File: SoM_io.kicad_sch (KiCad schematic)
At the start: 1 part, among them J1 Hermaphroditic_Molex_203456-0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

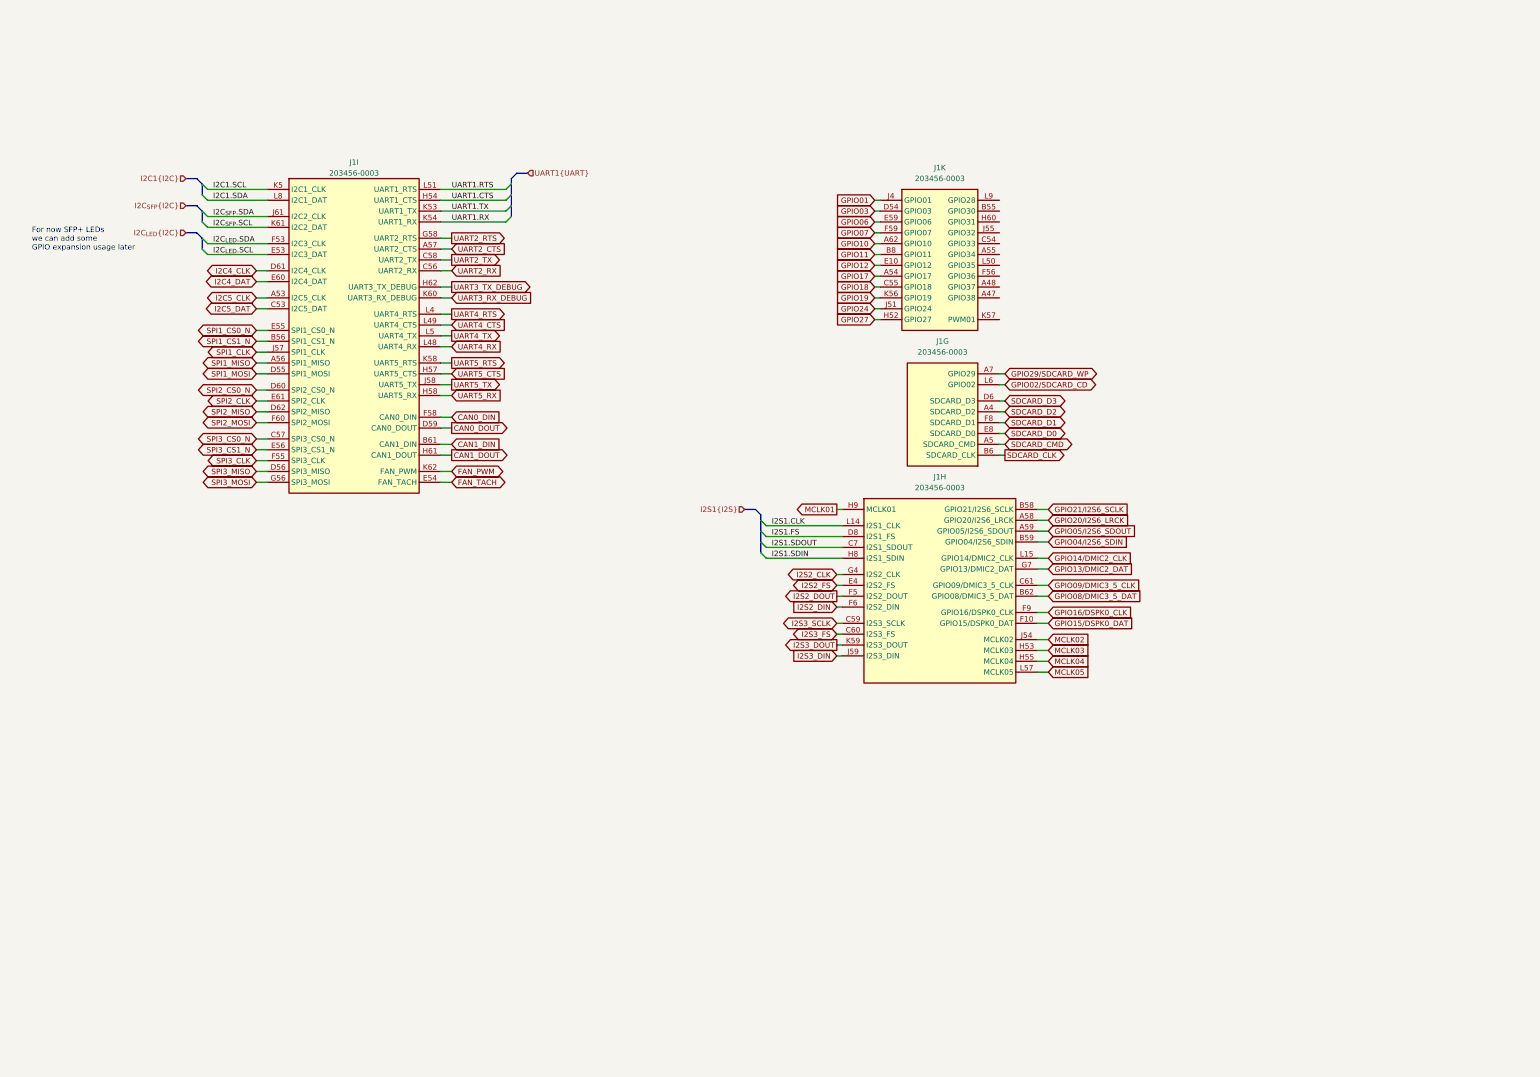
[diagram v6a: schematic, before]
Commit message: [#81970] Finalize connecting SFP+ to SOM
[#82054] Update SoM pins definitions

[#82054] Continue work on I2C

[#82330] Clean up

[#81970] Add SFP sheet and power section

[#82330] Annotation and clean up
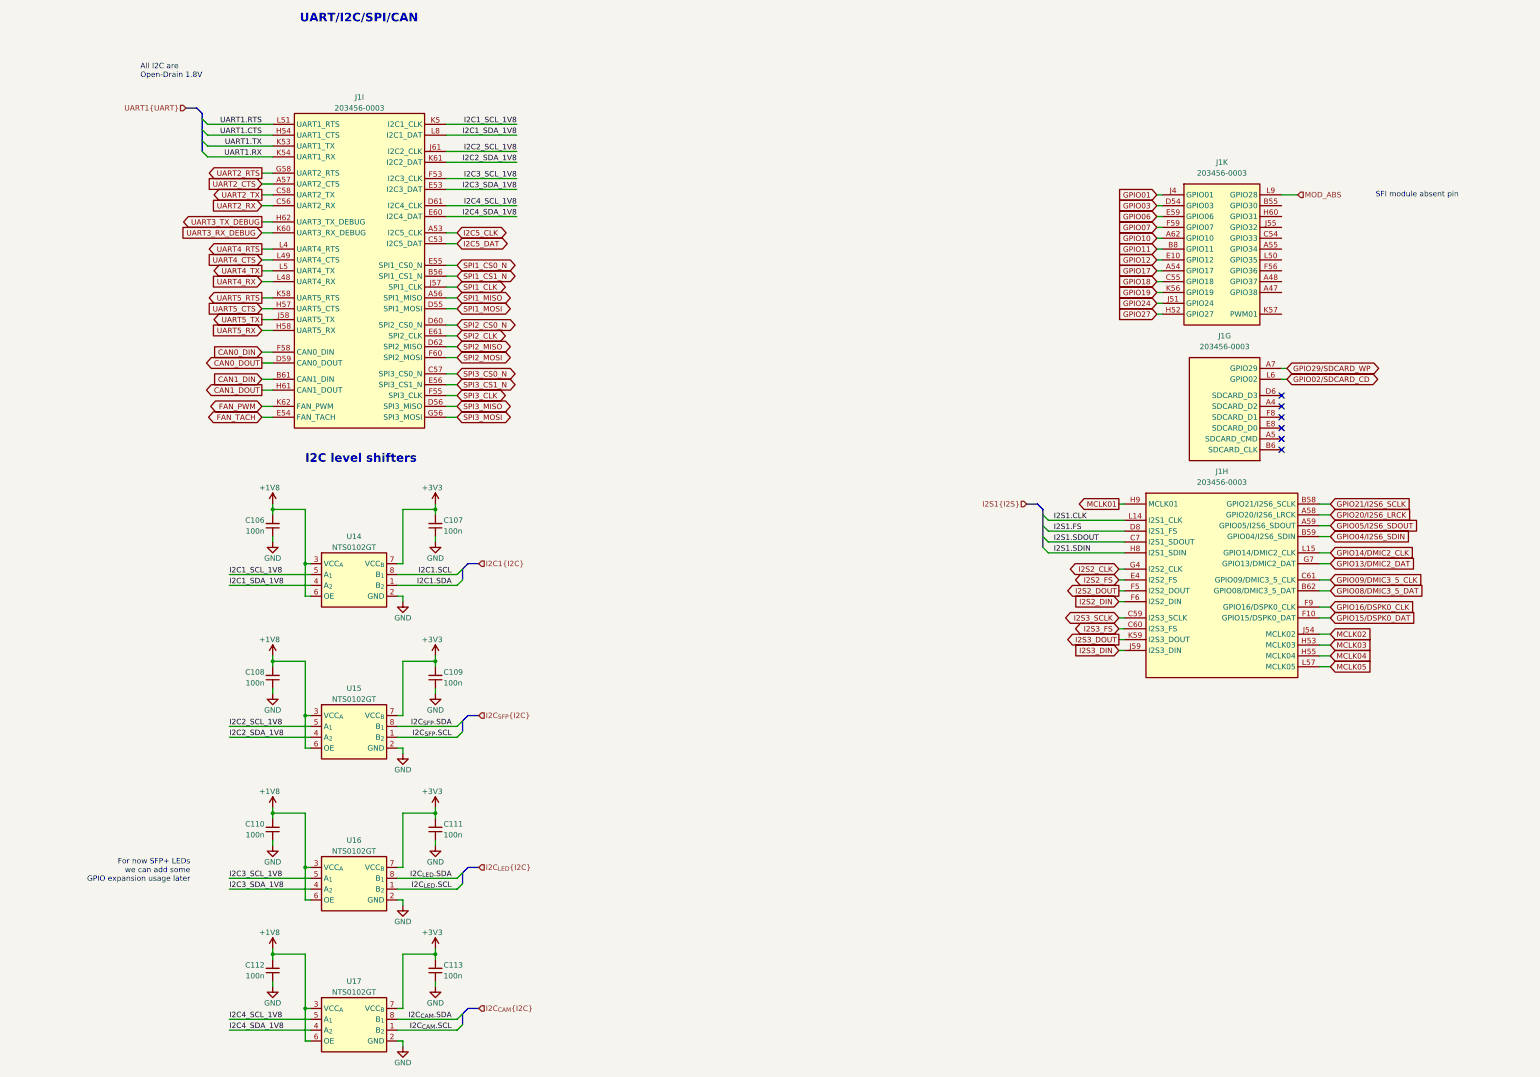
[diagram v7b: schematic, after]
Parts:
- added C106, C107, C108, C109, C110, C111, C112, C113: C_100n_0402, antmicro-footprints:C_0402_1005Metric, symbol antmicroCapacitors0402:C_100n_0402
- added U14, U15, U16, U17: NTS0102_XSON, antmicro-footprints:XSON-8_1x1.95mm_P0.5mm, symbol antmicroLogicTranslatorsLevelShifters:NTS0102_XSON
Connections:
- net I2C1.SCL: now also U14.8 (B_{1}); no longer J1.K5 (I2C1_CLK)
- net I2C1.SDA: now also U14.1 (B_{2}); no longer J1.L8 (I2C1_DAT)
- net I2C_{LED}.SCL: now also U16.1 (B_{2}); no longer J1.E53 (I2C3_DAT)
- net I2C_{LED}.SDA: now also U16.8 (B_{1}); no longer J1.F53 (I2C3_CLK)
- net I2C_{SFP}.SCL: now also U15.1 (B_{2}); no longer J1.K61 (I2C2_DAT)
- net I2C_{SFP}.SDA: now also U15.8 (B_{1}); no longer J1.J61 (I2C2_CLK)
- net MOD_ABS: now reaches J1.L9 (GPIO28)
- net I2C4_CLK renamed I2C4_SCL_1V8
- net I2C4_SCL_1V8: now also U17.5 (A_{1})
- net I2C4_DAT renamed I2C4_SDA_1V8
- net I2C4_SDA_1V8: now also U17.4 (A_{2})
- net SDCARD_CLK: no longer names the net of J1.B6 (SDCARD_CLK)
- net SDCARD_CMD: no longer names the net of J1.A5 (SDCARD_CMD)
- net SDCARD_D0: no longer names the net of J1.E8 (SDCARD_D0)
- net SDCARD_D1: no longer names the net of J1.F8 (SDCARD_D1)
- net SDCARD_D2: no longer names the net of J1.A4 (SDCARD_D2)
- net SDCARD_D3: no longer names the net of J1.D6 (SDCARD_D3)
- new net +1V8: C106.2, C108.2, C110.2, C112.2, U14.3 (VCC_{A}), U14.6 (OE), U15.3 (VCC_{A}), U15.6 (OE), U16.3 (VCC_{A}), U16.6 (OE), U17.3 (VCC_{A}), U17.6 (OE)
- new net +3V3: C107.2, C109.2, C111.2, C113.2, U14.7 (VCC_{B}), U15.7 (VCC_{B}), U16.7 (VCC_{B}), U17.7 (VCC_{B})
- new net GND: C106.1, C107.1, C108.1, C109.1, C110.1, C111.1, C112.1, C113.1, U14.2 (GND), U15.2 (GND), U16.2 (GND), U17.2 (GND)
- new net I2C1_SCL_1V8: J1.K5 (I2C1_CLK), U14.5 (A_{1})
- new net I2C1_SDA_1V8: J1.L8 (I2C1_DAT), U14.4 (A_{2})
- new net I2C2_SCL_1V8: J1.J61 (I2C2_CLK), U15.5 (A_{1})
- new net I2C2_SDA_1V8: J1.K61 (I2C2_DAT), U15.4 (A_{2})
- new net I2C3_SCL_1V8: J1.F53 (I2C3_CLK), U16.5 (A_{1})
- new net I2C3_SDA_1V8: J1.E53 (I2C3_DAT), U16.4 (A_{2})
- new net I2C_{CAM}.SCL: U17.1 (B_{2})
- new net I2C_{CAM}.SDA: U17.8 (B_{1})
- no-connect marks 0 -> 6
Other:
- note added: "All I2C are Open-Drain 1.8V"
- note added: "I2C level shifters"
- note added: "SFI module absent pin"
- note added: "UART/I2C/SPI/CAN"
- moved on the sheet: J1G, J1H, J1I, J1K

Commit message: [#81970] Route traces from root schematic on SoM schematics
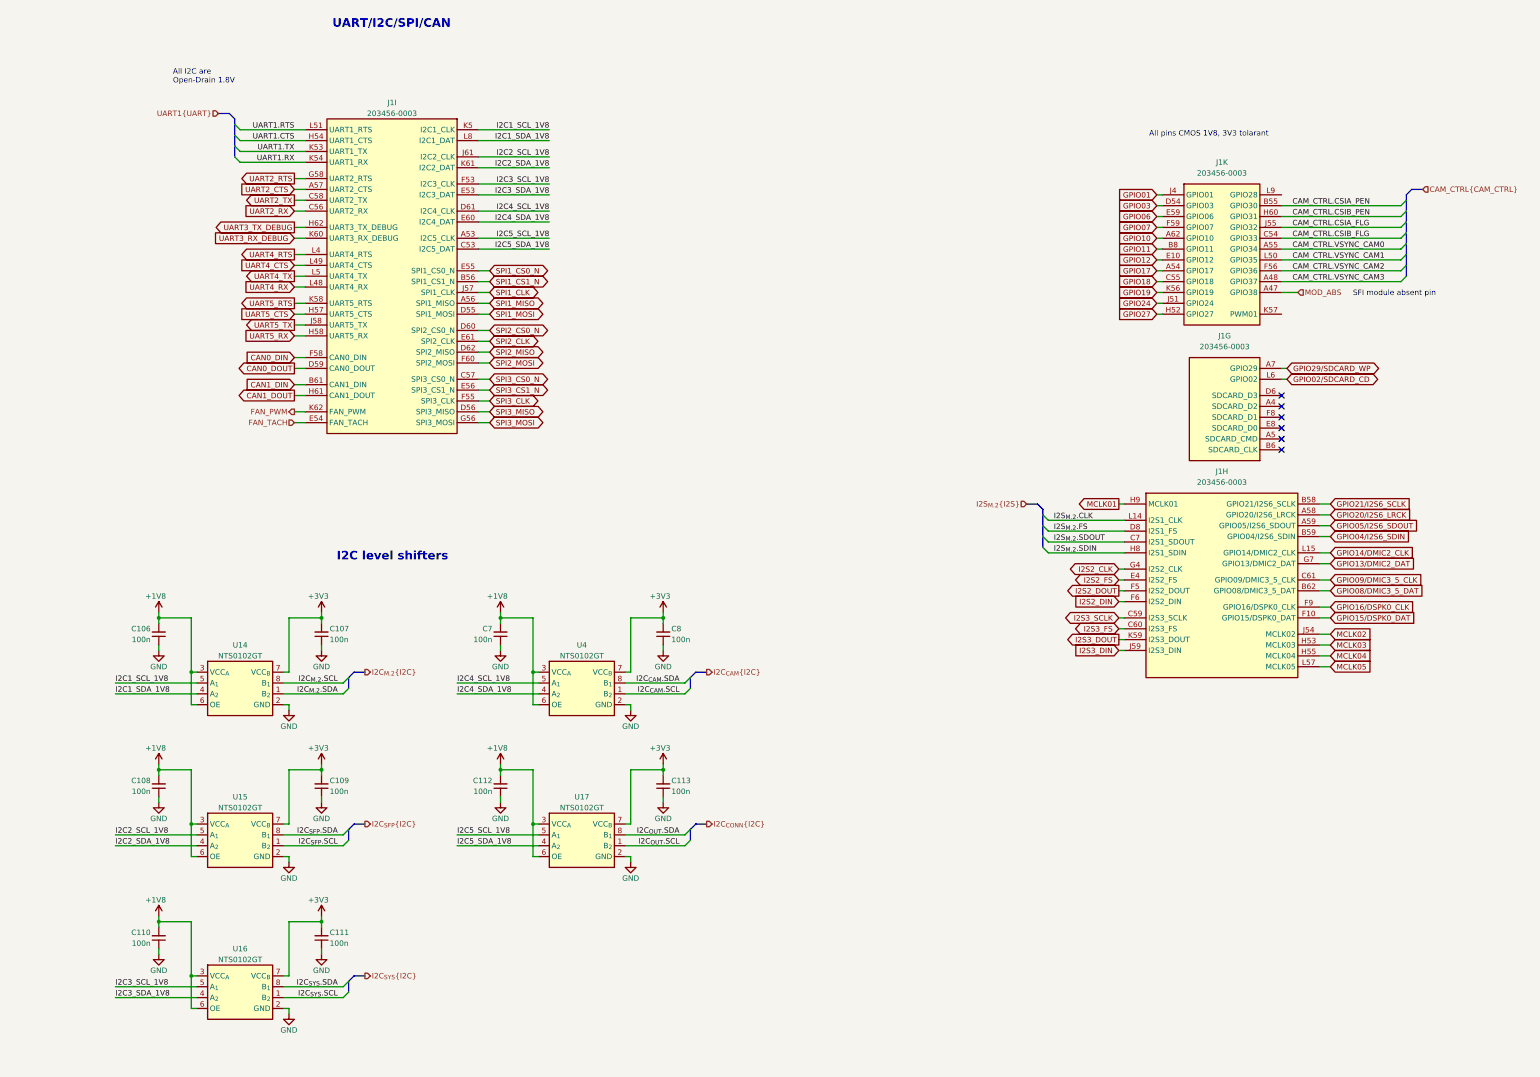
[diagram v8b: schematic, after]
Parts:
- added C7, C8: C_100n_0402, antmicro-footprints:C_0402_1005Metric, symbol antmicroCapacitors0402:C_100n_0402
- added U4: NTS0102_XSON, antmicro-footprints:XSON-8_1x1.95mm_P0.5mm, symbol antmicroLogicTranslatorsLevelShifters:NTS0102_XSON
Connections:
- net +1V8: now also C7.2, U4.3 (VCC_{A}), U4.6 (OE)
- net +3V3: now also C8.2, U4.7 (VCC_{B})
- net GND: now also C7.1, C8.1, U4.2 (GND)
- net I2C4_SCL_1V8: now also U4.5 (A_{1}); no longer U17.5 (A_{1})
- net I2C4_SDA_1V8: now also U4.4 (A_{2}); no longer U17.4 (A_{2})
- net I2C_{CAM}.SCL: now also U4.1 (B_{2}); no longer U17.1 (B_{2})
- net I2C_{CAM}.SDA: now also U4.8 (B_{1}); no longer U17.8 (B_{1})
- net MOD_ABS: now also J1.A47 (GPIO38); no longer J1.L9 (GPIO28)
- net CAM_CTRL.VSYNC_CAM3: now reaches J1.A48 (GPIO37)
- net CAM_CTRL.VSYNC_CAM0: now reaches J1.A55 (GPIO34)
- net CAM_CTRL.CSIA_PEN: now reaches J1.B55 (GPIO30)
- net CAM_CTRL.CSIB_FLG: now reaches J1.C54 (GPIO33)
- net CAM_CTRL.VSYNC_CAM2: now reaches J1.F56 (GPIO36)
- net CAM_CTRL.CSIB_PEN: now reaches J1.H60 (GPIO31)
- net CAM_CTRL.CSIA_FLG: now reaches J1.J55 (GPIO32)
- net CAM_CTRL.VSYNC_CAM1: now reaches J1.L50 (GPIO35)
- net I2C1.SCL renamed I2C_{M.2}.SCL
- net I2C1.SDA renamed I2C_{M.2}.SDA
- net I2C5_CLK renamed I2C5_SCL_1V8
- net I2C5_SCL_1V8: now also U17.5 (A_{1})
- net I2C5_DAT renamed I2C5_SDA_1V8
- net I2C5_SDA_1V8: now also U17.4 (A_{2})
- net I2C_{LED}.SCL renamed I2C_{SYS}.SCL
- net I2C_{LED}.SDA renamed I2C_{SYS}.SDA
- net I2S1.CLK renamed I2S_{M.2}.CLK
- net I2S1.FS renamed I2S_{M.2}.FS
- net I2S1.SDIN renamed I2S_{M.2}.SDIN
- net I2S1.SDOUT renamed I2S_{M.2}.SDOUT
- new net I2C_{OUT}.SCL: U17.1 (B_{2})
- new net I2C_{OUT}.SDA: U17.8 (B_{1})
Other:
- note added: "All pins CMOS 1V8, 3V3 tolarant"
- note removed: "For now SFP+ LEDs we can add some GPIO expansion usage later"
- moved on the sheet: C106, C107, C108, C109, C110, C111, C112, C113, J1I, U14, U15, U16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
